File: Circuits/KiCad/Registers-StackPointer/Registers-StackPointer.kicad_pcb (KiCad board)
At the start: 2 copper layers, 104.1 x 104.1 mm, 6 parts, among them J1 BUS1, J2 BUS2

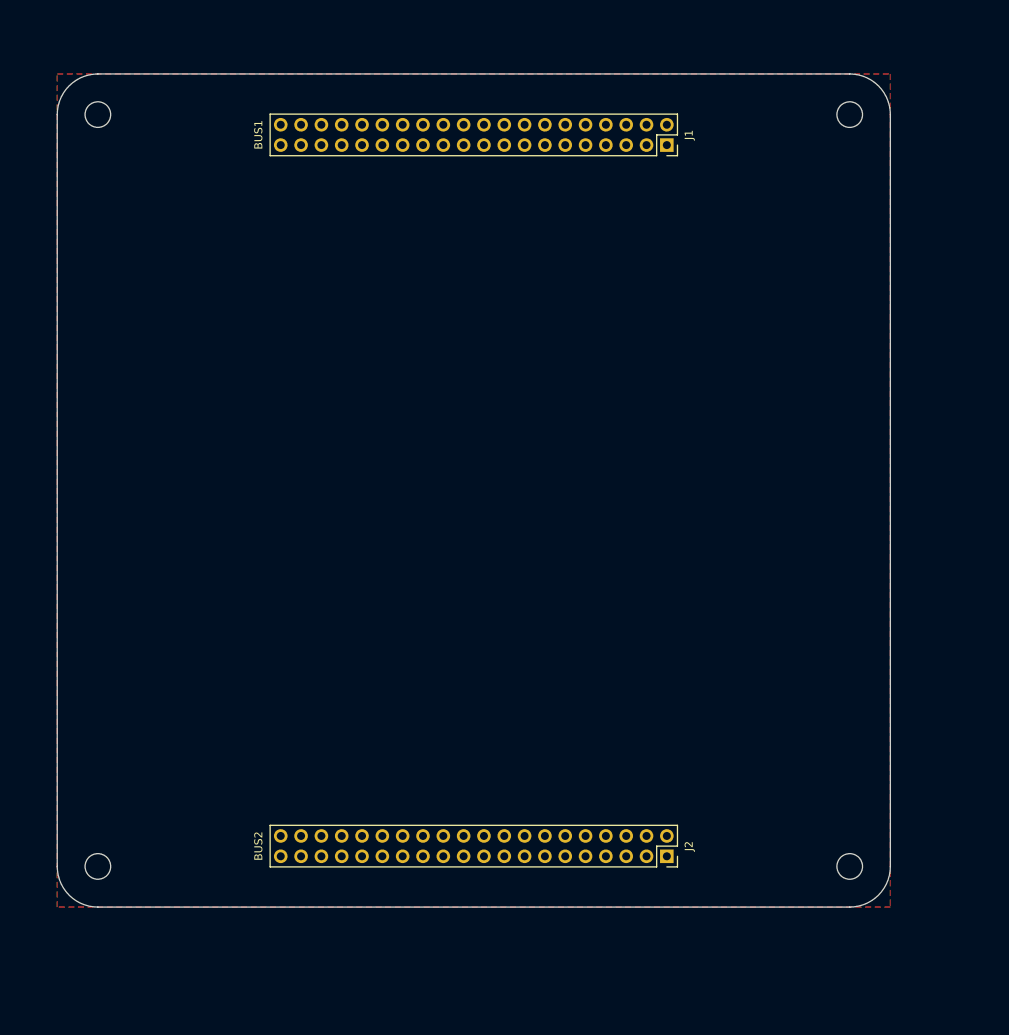
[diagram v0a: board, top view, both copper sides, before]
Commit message: Register/stack schematic & PCB
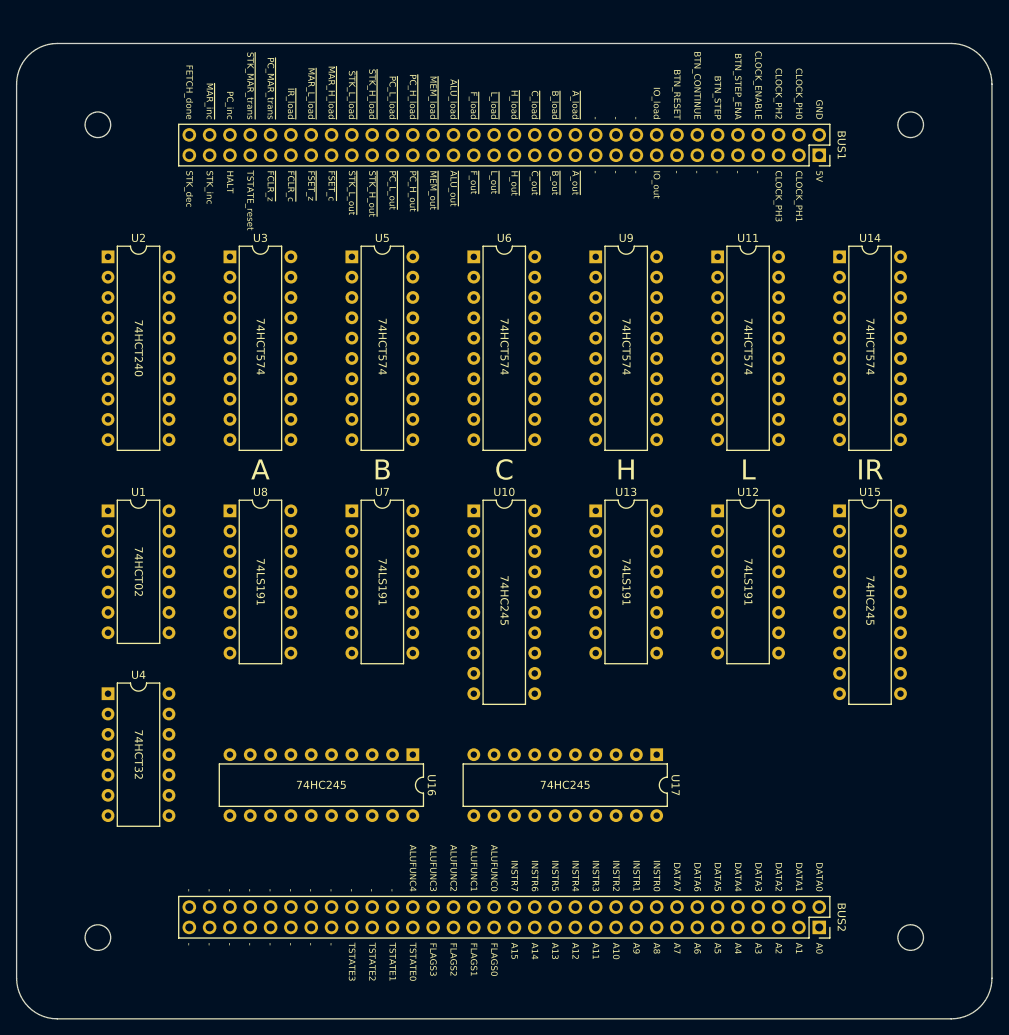
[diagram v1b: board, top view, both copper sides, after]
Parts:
- removed J1: BUS1, Connector_PinSocket_2.54mm:PinSocket_2x20_P2.54mm_Vertical
- removed J2: BUS2, Connector_PinSocket_2.54mm:PinSocket_2x20_P2.54mm_Vertical
- added BUS1: Conn_02x32_Odd_Even, Connector_PinSocket_2.54mm:PinSocket_2x32_P2.54mm_Vertical, F.Cu at (121.9, 36.8)
- added BUS2: Conn_02x32_Odd_Even, Connector_PinSocket_2.54mm:PinSocket_2x32_P2.54mm_Vertical, F.Cu at (121.9, 133.3)
- added U1: 74HCT02, Package_DIP:DIP-14_W7.62mm, F.Cu at (33.0, 81.3)
- added U10: 74HC245, Package_DIP:DIP-20_W7.62mm, F.Cu at (78.7, 81.3)
- added U11: 74HCT574, Package_DIP:DIP-20_W7.62mm, F.Cu at (109.2, 49.5)
- added U12: 74LS191, Package_DIP:DIP-16_W7.62mm, F.Cu at (109.2, 81.3)
- added U13: 74LS191, Package_DIP:DIP-16_W7.62mm, F.Cu at (94.0, 81.3)
- added U14: 74HCT574, Package_DIP:DIP-20_W7.62mm, F.Cu at (124.5, 49.5)
- added U15: 74HC245, Package_DIP:DIP-20_W7.62mm, F.Cu at (124.5, 81.3)
- added U16: 74HC245, Package_DIP:DIP-20_W7.62mm, F.Cu at (71.1, 111.8)
- added U17: 74HC245, Package_DIP:DIP-20_W7.62mm, F.Cu at (101.6, 111.8)
- added U2: 74HCT240, Package_DIP:DIP-20_W7.62mm, F.Cu at (33.0, 49.5)
- added U3: 74HCT574, Package_DIP:DIP-20_W7.62mm, F.Cu at (48.3, 49.5)
- added U4: 74HCT32, Package_DIP:DIP-14_W7.62mm, F.Cu at (33.0, 104.1)
- added U5: 74HCT574, Package_DIP:DIP-20_W7.62mm, F.Cu at (63.5, 49.5)
- added U6: 74HCT574, Package_DIP:DIP-20_W7.62mm, F.Cu at (78.7, 49.5)
- added U7: 74LS191, Package_DIP:DIP-16_W7.62mm, F.Cu at (63.5, 81.3)
- added U8: 74LS191, Package_DIP:DIP-16_W7.62mm, F.Cu at (48.3, 81.3)
- added U9: 74HCT574, Package_DIP:DIP-20_W7.62mm, F.Cu at (94.0, 49.5)
- moved H3 11.7 mm to (133.3, 134.6)
- moved H2 8.89 mm to (31.8, 134.6)
- moved H4 7.73 mm to (133.3, 33.0)
- moved H1 1.27 mm to (31.8, 33.0)
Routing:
- removed copper zone on F.Cu, net (none)
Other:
- board size 104.1 x 104.1 mm -> 121.9 x 121.9 mm
- board text added: "-"
- board text added: "5V"
- board text added: "A"
- board text added: "A0"
- board text added: "A1"
- board text added: "A10"
- board text added: "A11"
- board text added: "A12"
- board text added: "A13"
- board text added: "A14"
- board text added: "A15"
- board text added: "A2"
- board text added: "A3"
- board text added: "A4"
- board text added: "A5"
- board text added: "A6"
- board text added: "A7"
- board text added: "A8"
- board text added: "A9"
- board text added: "ALUFUNC0"
- board text added: "ALUFUNC1"
- board text added: "ALUFUNC2"
- board text added: "ALUFUNC3"
- board text added: "ALUFUNC4"
- board text added: "B"
- board text added: "BTN_CONTINUE"
- board text added: "BTN_RESET"
- board text added: "BTN_STEP"
- board text added: "BTN_STEP_ENA"
- board text added: "C"
- board text added: "CLOCK_ENABLE"
- board text added: "CLOCK_PH0"
- board text added: "CLOCK_PH1"
- board text added: "CLOCK_PH2"
- board text added: "CLOCK_PH3"
- board text added: "DATA0"
- board text added: "DATA1"
- board text added: "DATA2"
- board text added: "DATA3"
- board text added: "DATA4"
- board text added: "DATA5"
- board text added: "DATA6"
- board text added: "DATA7"
- board text added: "DM-02 | Registers & Stack | Revision 1"
- board text added: "FETCH_done"
- board text added: "FLAGS0"
- board text added: "FLAGS1"
- board text added: "FLAGS2"
- board text added: "FLAGS3"
- board text added: "GND"
- board text added: "H"
- board text added: "HALT"
- board text added: "INSTR0"
- board text added: "INSTR1"
- board text added: "INSTR2"
- board text added: "INSTR3"
- board text added: "INSTR4"
- board text added: "INSTR5"
- board text added: "INSTR6"
- board text added: "INSTR7"
- board text added: "IO_load"
- board text added: "IO_out"
- board text added: "IR"
- board text added: "L"
- board text added: "PC_inc"
- board text added: "STK_dec"
- board text added: "STK_inc"
- board text added: "TSTATE0"
- board text added: "TSTATE1"
- board text added: "TSTATE2"
- board text added: "TSTATE3"
- board text added: "TSTATE_reset"
- board text added: "https://dutchmaker.com"
- board text added: "~ALU_load"
- board text added: "~ALU_out"
- board text added: "~A_load"
- board text added: "~A_out"
- board text added: "~B_load"
- board text added: "~B_out"
- board text added: "~C_load"
- board text added: "~C_out"
- board text added: "~FCLR_c"
- board text added: "~FCLR_z"
- board text added: "~FSET_c"
- board text added: "~FSET_z"
- board text added: "~F_load"
- board text added: "~F_out"
- board text added: "~H_load"
- board text added: "~H_out"
- board text added: "~IR_load"
- board text added: "~L_load"
- board text added: "~L_out"
- board text added: "~MAR_H_load"
- board text added: "~MAR_L_load"
- board text added: "~MAR_inc"
- board text added: "~MEM_load"
- board text added: "~MEM_out"
- board text added: "~PC_H_load"
- board text added: "~PC_H_out"
- board text added: "~PC_L_load"
- board text added: "~PC_L_out"
- board text added: "~PC_MAR_trans"
- board text added: "~STK_H_load"
- board text added: "~STK_H_out"
- board text added: "~STK_L_load"
- board text added: "~STK_L_out"
- board text added: "~STK_MAR_trans"
- board text removed: "Revision 1"
- board text removed: "https://github.com/DutchMaker/DM-02"

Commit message: Did a bit of work on circuit design
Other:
- board text added: "STACK H"
- board text added: "STACK L"
